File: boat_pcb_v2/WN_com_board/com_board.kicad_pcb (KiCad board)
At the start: 2 copper layers, 62 parts, among them J1 Conn_01x26_Socket, J2 USB_C_Receptacle_USB2.0_16P, J5 Conn_01x26_Socket, J7 XBP9B-DMUTB002, J8 Conn_01x02_Pin, J9 Conn_01x26_Socket, Q1 NMOS, U1 Particle_B404X, U2 AP62301WU-7, U3 AP62301WU-7

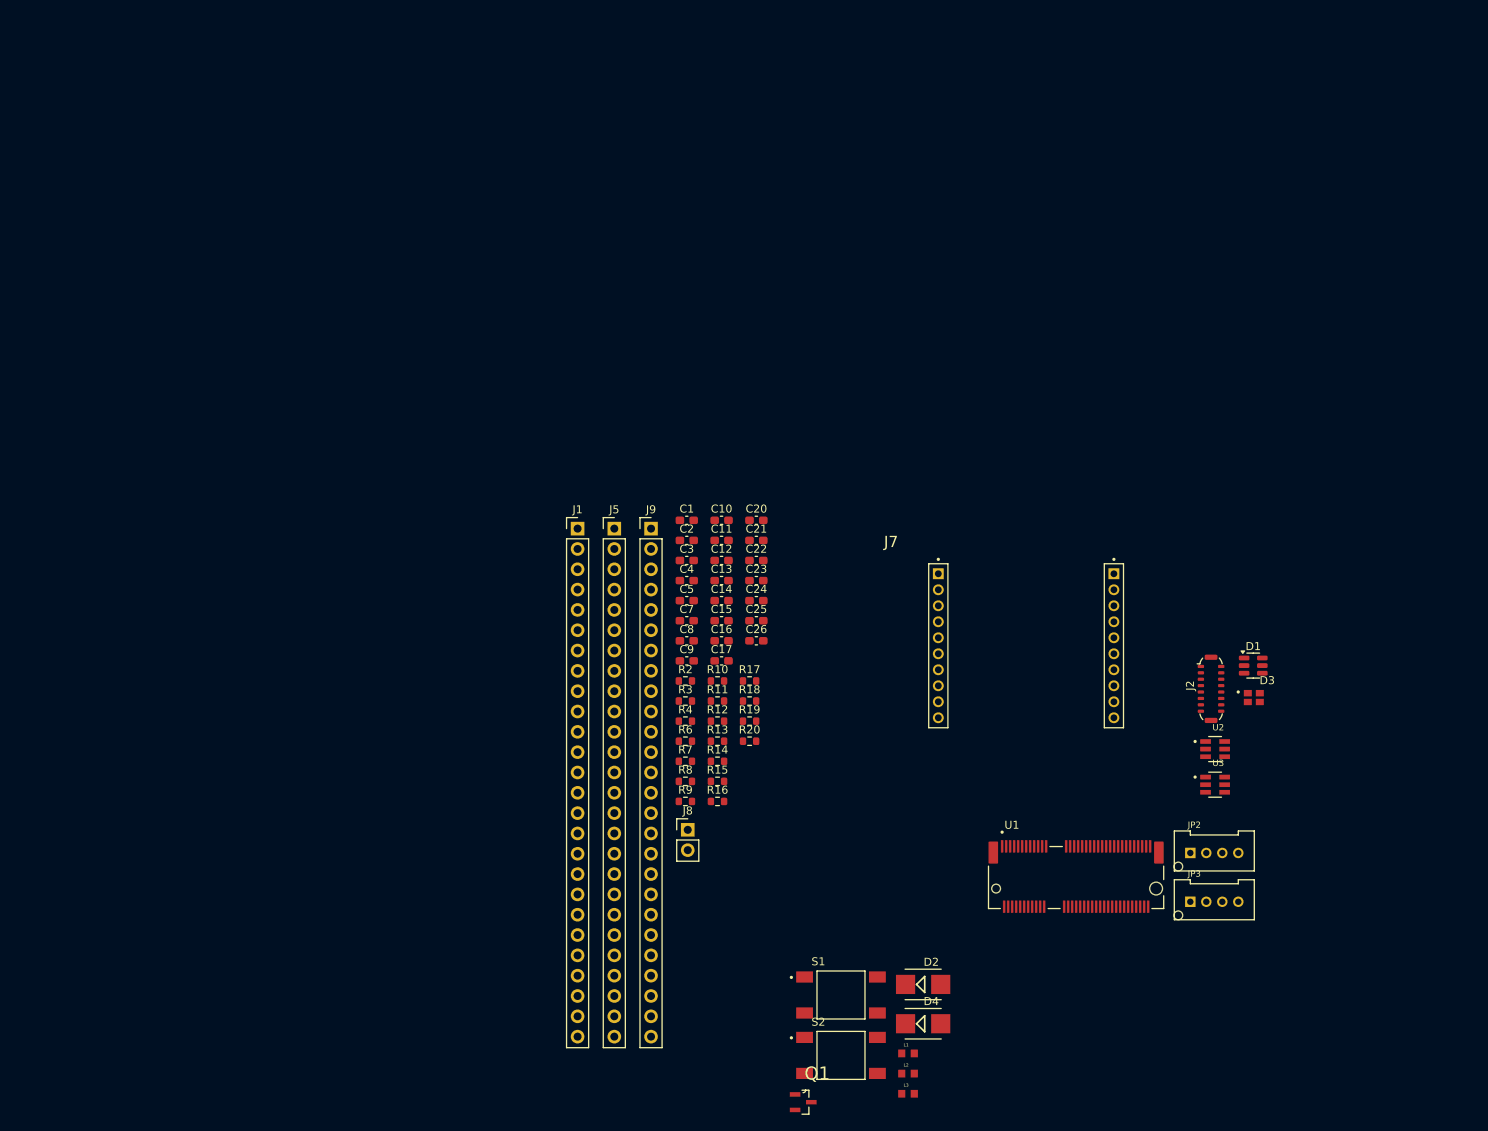
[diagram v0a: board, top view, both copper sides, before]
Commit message: minor updates related to board layout
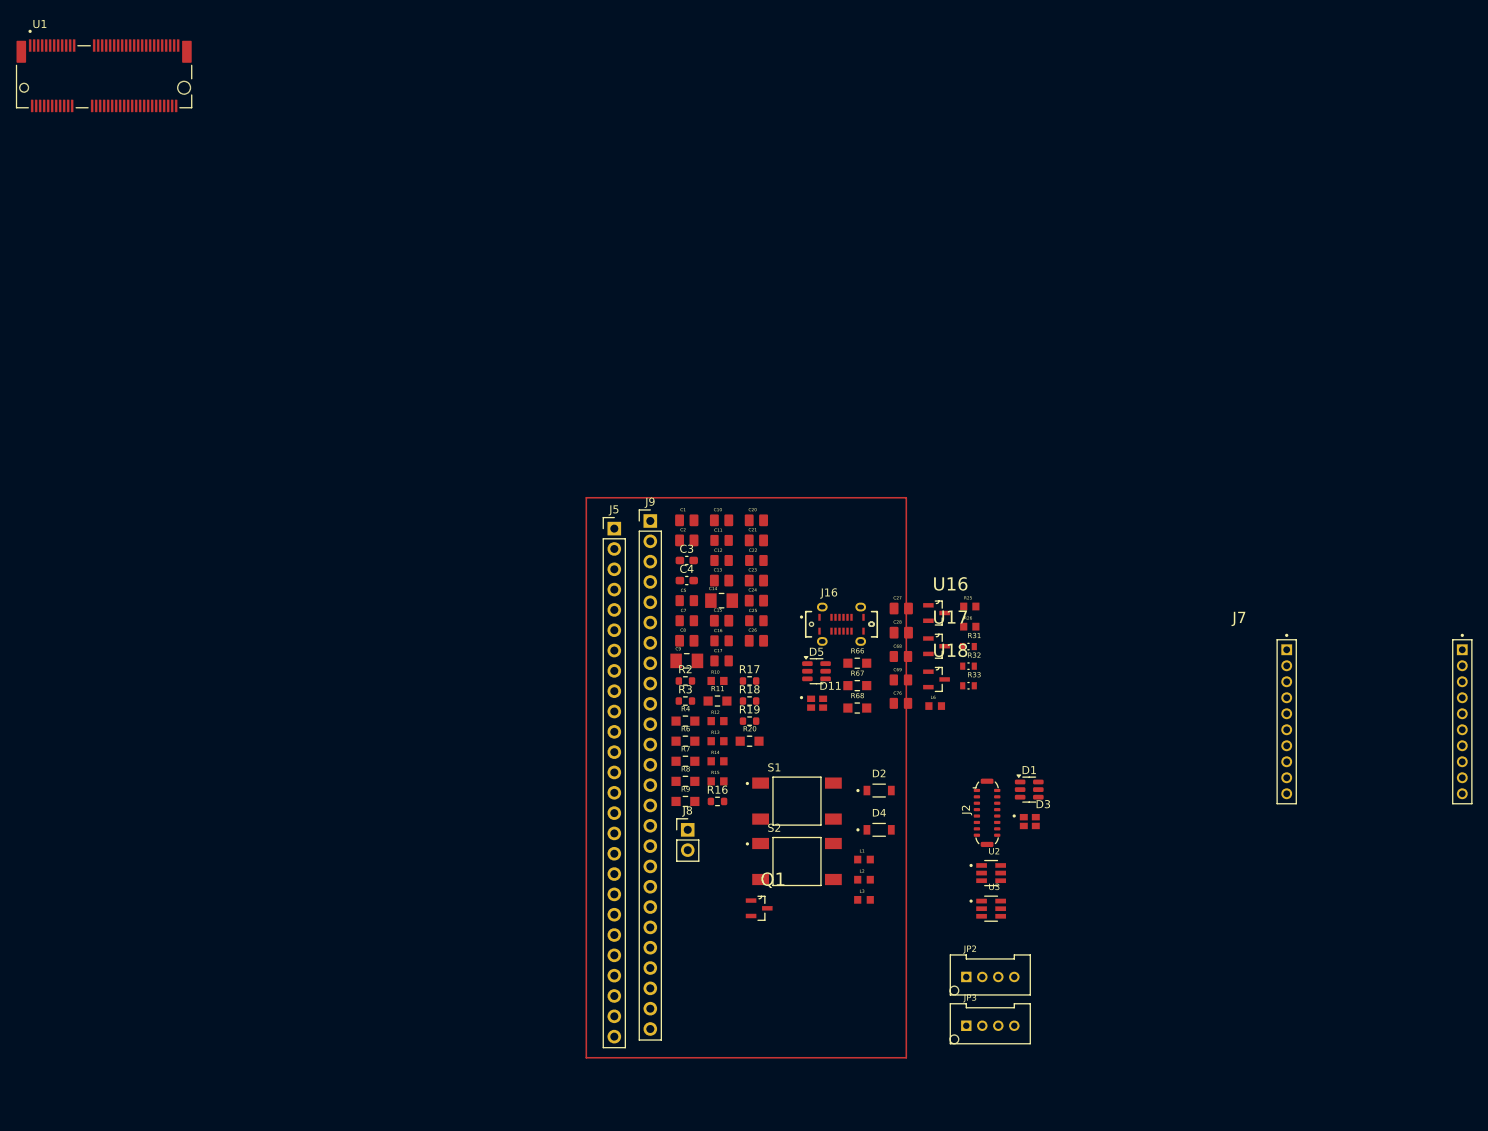
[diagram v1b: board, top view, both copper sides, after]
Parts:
- removed J1: Conn_01x26_Socket, Connector_PinHeader_2.54mm:PinHeader_1x26_P2.54mm_Vertical
- added C27: 1µ, 100V, WaterNet26 Footprints:CAPC2012X145N, F.Cu at (110.9, 72.3)
- added C28: 1µ, 100V, WaterNet26 Footprints:CAPC2012X145N, F.Cu at (110.9, 75.4)
- added C68: 0.1uF 25V, WaterNet26 Footprints:CAPC2012X95N, F.Cu at (110.8, 78.3)
- added C69: 0.1uF 25V, WaterNet26 Footprints:CAPC2012X95N, F.Cu at (110.8, 81.3)
- added C76: 0.1uF 25V, WaterNet26 Footprints:CAPC2012X95N, F.Cu at (110.8, 84.2)
- added D11: CLMVC-FKA-CL1D1L71BB7C3C3, WaterNet26 Footprints:LED_CLMVC-FKA-CL1D1L71BB7C3C3, F.Cu at (100.3, 84.2)
- added D5: USBLC6-2SC6, Package_TO_SOT_SMD:SOT-23-6, F.Cu at (100.3, 80.2)
- added J16: USB4120-03-C_REVA6, WaterNet26 Footprints:GCT_USB4120-03-C_REVA6, F.Cu at (103.4, 74.3)
- added L6: 3.3µ, WaterNet26 Footprints:INDC1608X95N, F.Cu at (115.1, 84.5)
- added R25: 5.1K, WaterNet26 Footprints:RESC1508X55N, F.Cu at (119.4, 72.1)
- added R26: 5.1K, WaterNet26 Footprints:RESC1508X55N, F.Cu at (119.4, 74.6)
- added R31: 100 Ohm, WaterNet26 Footprints:RES_ERJ3EKF1000V, F.Cu at (119.3, 77.1)
- added R32: 100 Ohm, WaterNet26 Footprints:RES_ERJ3EKF1000V, F.Cu at (119.3, 79.5)
- added R33: 100 Ohm, WaterNet26 Footprints:RES_ERJ3EKF1000V, F.Cu at (119.3, 82.0)
- added R66: 10K, WaterNet26 Footprints:RES_ERA6AEB103V, F.Cu at (105.4, 79.2)
- added R67: 10K, WaterNet26 Footprints:RES_ERA6AEB103V, F.Cu at (105.4, 82.0)
- added R68: 10K, WaterNet26 Footprints:RES_ERA6AEB103V, F.Cu at (105.4, 84.8)
- added U16: BSS123-7-F, WaterNet26 Footprints:SOT95P240X110-3N, F.Cu at (115.3, 72.9)
- added U17: BSS123-7-F, WaterNet26 Footprints:SOT95P240X110-3N, F.Cu at (115.3, 77.1)
- added U18: BSS123-7-F, WaterNet26 Footprints:SOT95P240X110-3N, F.Cu at (115.3, 81.2)
- C1, C2, C20, C21, C26: value 1µ, 25V -> 1µ, 100V; footprint Capacitor_SMD:C_0603_1608Metric_Pad1.08x0.95mm_HandSolder -> WaterNet26 Footprints:CAPC2012X145N
- C10, C13, C15, C23, C24, C8: footprint Capacitor_SMD:C_0603_1608Metric_Pad1.08x0.95mm_HandSolder -> WaterNet26 Footprints:CAPC2012X145N
- C11, C12, C16, C17, C22, C25, C5, C7: footprint Capacitor_SMD:C_0603_1608Metric_Pad1.08x0.95mm_HandSolder -> WaterNet26 Footprints:CAPC2012X95N
- C14, C9: footprint Capacitor_SMD:C_0603_1608Metric_Pad1.08x0.95mm_HandSolder -> WaterNet26 Footprints:CAPC3216X180N
- D2, D4: value D_Schottky -> RB070MM-30TR; footprint WN_com_board:SMB -> WaterNet26 Footprints:DIO_RB070MM-30TR
- J7: footprint WN_com_board:SULLINS_NPPN101BFCN-RC -> WaterNet26 Footprints:SULLINS_NPPN101BFCN-RC
- JP2, JP3: footprint WN_com_board:B04B-PASK-1 -> WaterNet26 Footprints:B04B-PASK-1
- L1, L2: footprint WN_com_board:INDC1608X95N -> WaterNet26 Footprints:INDC1608X95N
- Q1: footprint WN_com_board:SOT95P240X110-3N -> WaterNet26 Footprints:SOT95P240X110-3N
- R10, R12, R13, R14, R15: footprint Resistor_SMD:R_0603_1608Metric -> WaterNet26 Footprints:RESC1608X55N
- R11, R8: footprint Resistor_SMD:R_0603_1608Metric -> WaterNet26 Footprints:RES_ERA6AEB103V
- R20, R4, R6, R9: footprint Resistor_SMD:R_0603_1608Metric -> WaterNet26 Footprints:RES_ERA6AEB104V
- R7: footprint Resistor_SMD:R_0603_1608Metric -> WaterNet26 Footprints:RES_ERA6AEB3162V
- S1, S2: footprint WN_com_board:SW_TS04-66-50-BK-160-SMT-TR -> WaterNet26 Footprints:SW_TS04-66-50-BK-160-SMT-TR
- U1: footprint WN_com_board:b404x -> WaterNet26 Footprints:b404x
- U2, U3: footprint WN_com_board:SOT95P280X100-6N -> WaterNet26 Footprints:SOT95P280X100-6N
- moved U1 157.4 mm to (11.2, 7.25)
- moved J7 44.6 mm to (159.0, 76.0)
- moved D1 32.0 mm to (126.9, 95.0)
- moved D3 32.0 mm to (126.9, 99.0)
- moved J2 32.0 mm to (121.6, 97.9)
- moved JP2 32.0 mm to (122.0, 118.4)
- moved JP3 32.0 mm to (122.0, 124.5)
- moved U2 32.0 mm to (122.1, 105.4)
- moved U3 32.0 mm to (122.1, 109.9)
- moved D2 24.9 mm to (108.1, 95.1)
- moved S2 24.9 mm to (97.8, 104.0)
- moved D4 24.9 mm to (108.1, 100.0)
- moved L1 24.9 mm to (106.2, 103.7)
- moved L3 24.9 mm to (106.2, 108.8)
- moved Q1 24.9 mm to (93.1, 109.8)
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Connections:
- C5 pad 1: /MODE -> /RESET
- R4 pad 2: /MODE -> /RESET
- S1 pad 1: /MODE -> /RESET
- S1 pad 3: /MODE -> /RESET
- U1 pad 23: unconnected-(U1-A0-Pad23) -> /A0
- U1 pad 61: /RGBR -> /RGB_R
- U1 pad 63: /RGBG -> /RGB_G
- U1 pad 65: /RGBB -> /RGB_B
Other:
- board outline added: 0.7 x 0.5 mm
